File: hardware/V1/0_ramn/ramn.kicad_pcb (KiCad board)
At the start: 2 copper layers, 85.6 x 54 mm, 106 parts, among them J1 USB_C_Micro, J2 Screw_Terminal_01x03, J3 , J4 , J5 , J6 , U1 ATA6561-GAQW-N, U10 ATA6561-GAQW-N, U11 STM32L443CCTx, U12 NCV8163, U2 STM32L443CCTx, U3 NCV8163, U4 ATA6561-GAQW-N, U5 STM32L443CCTx, U6 NCV8163, U7 ATA6561-GAQW-N, U8 STM32L443CCTx, U9 NCV8163, Y1 NX3225GD-8MHZ-STD-CRA-3, Y2 NX3225GD-8MHZ-STD-CRA-3, Y3 NX3225GD-8MHZ-STD-CRA-3, Y4 NX3225GD-8MHZ-STD-CRA-3

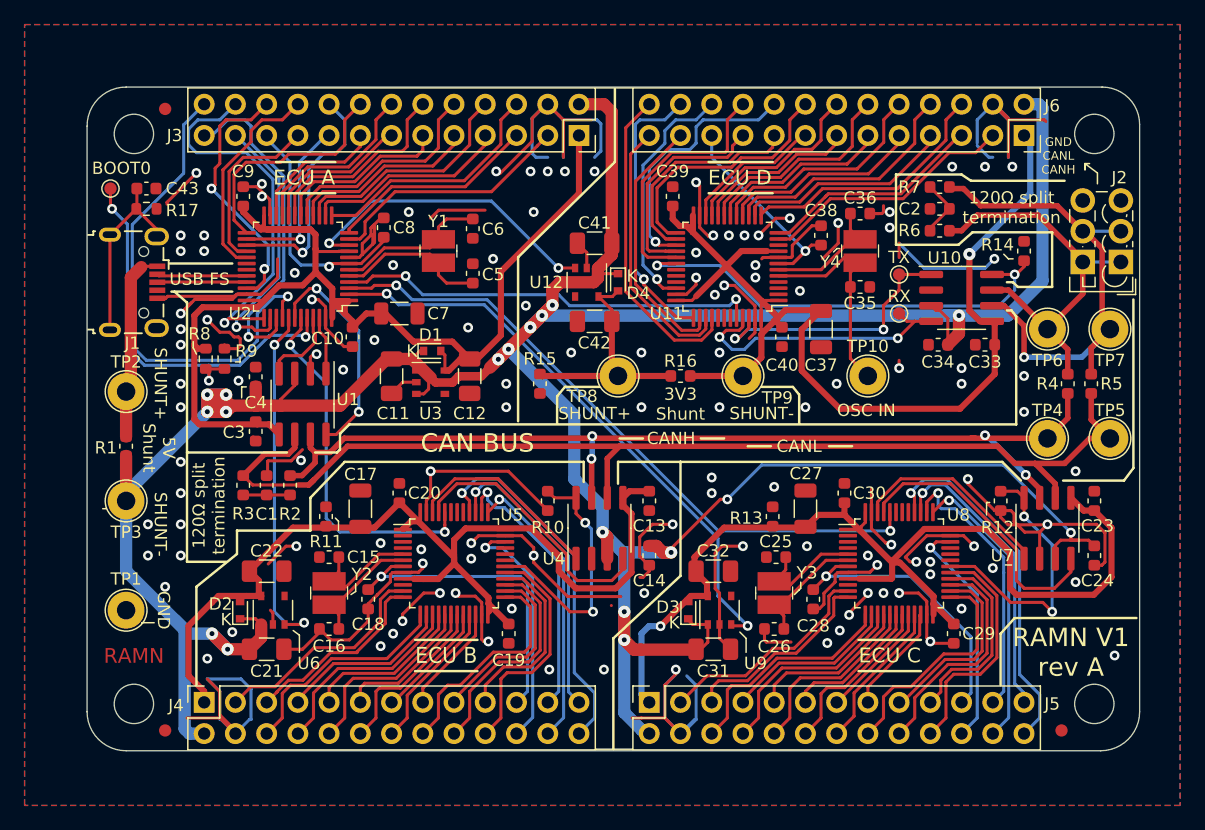
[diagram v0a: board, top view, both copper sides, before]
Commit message: Added initial V1 Firmware and Scripts
- Minor hardware fixes
- Minor documentation fixes
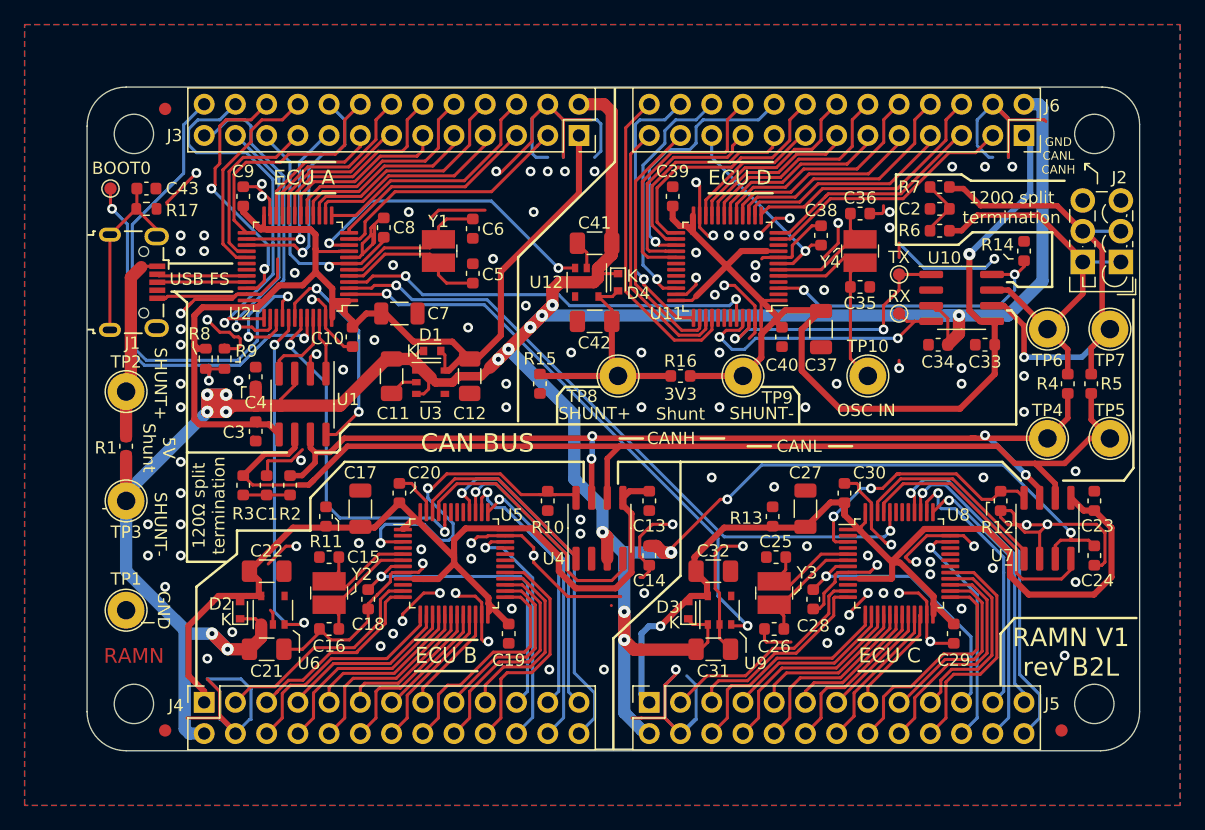
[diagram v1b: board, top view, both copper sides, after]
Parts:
- C1, C2: value 1nF -> 4.7nF
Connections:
- U11 pad 3: Net-(U11-Pad3) -> /ECUD/CAN_STB
- U11 pad 30: /ECUD/CAN_STB -> Net-(U11-Pad30)
- U5 pad 3: Net-(U5-Pad3) -> /ECUB/CAN_STB
- U5 pad 30: /ECUB/CAN_STB -> Net-(U5-Pad30)
- U8 pad 3: Net-(U8-Pad3) -> /ECUC/CAN_STB
- U8 pad 30: /ECUC/CAN_STB -> Net-(U8-Pad30)
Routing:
- net GND: track 345.3 -> 332.8 mm, vias 120 -> 121
- net /ECUD/CAN_STB: track 37.2 -> 25.0 mm
- net /ECUB/CAN_STB: track 21.0 -> 28.6 mm
- net /ECUC/CAN1_RX: track 23.2 -> 22.1 mm
- net /ECUC/3V3_ECU: track 84.9 -> 85.7 mm
- net /ECUB/BOOT0: track 29.6 -> 29.0 mm
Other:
- board text added: "RAMN V1 rev B2L"
- board text removed: "RAMN V1 rev A"
